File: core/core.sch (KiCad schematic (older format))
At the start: 141 parts, among them K0 KEYSW, K1 KEYSW, K10 KEYSW, K11 KEYSW, K12 KEYSW, K13 KEYSW, K14 KEYSW, K15 KEYSW, K16 KEYSW, K17 KEYSW, K18 KEYSW, K19 KEYSW, K2 KEYSW, K20 KEYSW, K21 KEYSW, K22 KEYSW, K23 KEYSW, K24 KEYSW, K25 KEYSW, K26 KEYSW, K27 KEYSW, K28 KEYSW, K29 KEYSW, K3 KEYSW, K30 KEYSW, K31 KEYSW, K32 KEYSW, K33 KEYSW, K34 KEYSW, K35 KEYSW, K36 KEYSW, K37 KEYSW, K38 KEYSW, K39 KEYSW, K4 KEYSW, K40 KEYSW, K41 KEYSW, K42 KEYSW, K43 KEYSW, K44 KEYSW, K45 KEYSW, K46 KEYSW, K47 KEYSW, K48 KEYSW, K49 KEYSW, K5 KEYSW, K50 KEYSW, K51 KEYSW, K52 KEYSW, K53 KEYSW, K54 KEYSW, K55 KEYSW, K56 KEYSW, K57 KEYSW, K58 KEYSW, K59 KEYSW, K6 KEYSW, K60 KEYSW, K61 KEYSW, K62 KEYSW, K63 KEYSW, K64 KEYSW, K65 KEYSW, K66 KEYSW, K67 KEYSW, K68 KEYSW, K69 KEYSW, K7 KEYSW, K8 KEYSW, K9 KEYSW, U1 TEENSY2.0

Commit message: finish keymatrix and assign footprints
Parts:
- D0, D1, D10, D11, D12, D13, D14, D15, D16, D17, D18, D19, D2, D20, D21, D22, D23, D24, D25, D26, D27, D28, D29, D3, D30, D31, D32, D33, D34, D35, D36, D37, D38, D39, D4, D40, D41, D42, D43, D44, D45, D46, D47, D48, D49, D5, D50, D51, D52, D53, D54, D55, D56, D57, D58, D59, D6, D60, D61, D62, D63, D64, D65, D66, D67, D68, D69, D7, D8, D9: footprint (none) -> keyboard_parts:D_SOD123_axial
- K0, K1, K10, K11, K12, K13, K14, K15, K16, K17, K18, K19, K2, K20, K21, K22, K23, K24, K25, K26, K27, K28, K29, K3, K30, K31, K32, K33, K34, K35, K36, K37, K38, K39, K4, K40, K41, K42, K43, K44, K45, K46, K47, K48, K49, K5, K50, K51, K52, K53, K54, K55, K56, K57, K58, K59, K6, K60, K61, K62, K63, K64, K65, K66, K67, K68, K69, K7, K8, K9: footprint (none) -> keyswitches:Kailh_socket
- U1: footprint (none) -> keebs:Teensy_20
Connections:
- wire segments 329 -> 439

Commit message: add an RGB controller to core
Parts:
- added U2: TLC5971PWP, Package_SO:HTSSOP-20-1EP_4.4x6.5mm_P0.65mm_EP3.4x6.5mm_Mask2.75x3.43mm_ThermalVias, symbol Driver_LED:TLC5971PWP
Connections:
- wire segments 439 -> 440
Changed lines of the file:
@@
 Wire Wire Line
 	9350 3050 10200 3050
+$Comp
+L Driver_LED:TLC5971PWP U2
+U 1 1 5DB64F07
+P 3150 4950
+F 0 "U2" H 3150 4061 50  0000 C CNN
+F 1 "TLC5971PWP" H 3150 3970 50  0000 C CNN
+F 2 "Package_SO:HTSSOP-20-1EP_4.4x6.5mm_P0.65mm_EP3.4x6.5mm_Mask2.75x3.43mm_ThermalVias" H 3200 4100 50  0001 L CNN
+F 3 "http://www.ti.com/lit/ds/symlink/tlc5971.pdf" H 3150 4650 50  0001 C CNN
+	1    3150 4950
+	1    0    0    -1
+$EndComp
+Wire Wire Line
+	2750 4850 2050 4850
 $EndSCHEMATC

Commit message: work on rgb stuff
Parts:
- added LED0, LED1, LED2, LED3, LED4, LED? (x70): LED_RGBC, symbol Device:LED_RGBC
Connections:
- net labels added: B_Zone0, G_Zone0, R_Zone0
- wire segments 440 -> 443

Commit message: update schematic with more addressable stuff
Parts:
- added D?: Inolux_IN-PI554FCH, LED_SMD:LED_Inolux_IN-PI554FCH_PLCC4_5.0x5.0mm_P3.2mm, symbol LED:Inolux_IN-PI554FCH
- D0, D1, D10, D11, D12, D13, D14, D15, D16, D17, D18, D19, D2, D20, D21, D22, D23, D24, D25, D26, D27, D28, D29, D3, D30, D31, D32, D33, D34, D35, D36, D37, D38, D39, D4, D40, D41, D42, D43, D44, D45, D46, D47, D48, D49, D5, D50, D51, D52, D53, D54, D55, D56, D57, D58, D59, D6, D60, D61, D62, D63, D64, D65, D66, D67, D68, D69, D7, D8, D9: symbol keyboard_parts:D -> core-rescue:D-keyboard_parts
- K0, K1, K10, K11, K12, K13, K14, K15, K16, K17, K18, K19, K2, K20, K21, K22, K23, K24, K25, K26, K27, K28, K29, K3, K30, K31, K32, K33, K34, K35, K36, K37, K38, K39, K4, K40, K41, K42, K43, K44, K45, K46, K47, K48, K49, K5, K50, K51, K52, K53, K54, K55, K56, K57, K58, K59, K6, K60, K61, K62, K63, K64, K65, K66, K67, K68, K69, K7, K8, K9: symbol keyboard_parts:KEYSW -> core-rescue:KEYSW-keyboard_parts
- U1: symbol keyboard_parts:TEENSY2.0 -> core-rescue:TEENSY2.0-keyboard_parts
- gave numbers to parts that had none: 29
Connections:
- net labels added: GND
- wire segments 443 -> 487
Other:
- moved on the sheet: LED0, LED1, LED10, LED11, LED12, LED13, LED14, LED15, LED16, LED17, LED18, LED19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

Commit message: add sources for LEDs and wire some in score schematic
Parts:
- removed D?: Inolux_IN-PI554FCH, LED_SMD:LED_Inolux_IN-PI554FCH_PLCC4_5.0x5.0mm_P3.2mm, symbol LED:Inolux_IN-PI554FCH
- removed LED0, LED1, LED10, LED11, LED12, LED13, LED14, LED15, LED16, LED17, LED18, LED19, LED2, LED20, LED21, LED22, LED23, LED24, LED25, LED26, LED27, LED28, LED29, LED3, LED30, LED31, LED32, LED33, LED4, LED5, LED6, LED7, LED8, LED9, LED? (x41): LED_RGBC, symbol Device:LED_RGBC
- removed U2: TLC5971PWP, Package_SO:HTSSOP-20-1EP_4.4x6.5mm_P0.65mm_EP3.4x6.5mm_Mask2.75x3.43mm_ThermalVias, symbol Driver_LED:TLC5971PWP
- added LED0, LED? (x24): WS2812, LED_SMD:LED_WS2812B_PLCC4_5.0x5.0mm_P3.2mm, symbol LED:WS2812B
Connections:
- net VCC_LED: now reaches U1.14 (VCC)
- net VCC_LED: now also LED0.3 (VSS), LED?.3 (VSS), LED?.3 (VSS), LED?.3 (VSS), LED?.3 (VSS), LED?.3 (VSS), LED?.3 (VSS), LED?.3 (VSS), LED?.3 (VSS), LED?.3 (VSS), LED?.3 (VSS), LED?.3 (VSS), LED?.3 (VSS), LED?.3 (VSS), LED?.3 (VSS), LED?.3 (VSS), LED?.3 (VSS), LED?.3 (VSS), LED?.3 (VSS), LED?.3 (VSS), LED?.3 (VSS), LED?.3 (VSS), LED?.3 (VSS), LED?.3 (VSS), LED?.3 (VSS)
- new net: LED0.2 (DOUT), LED?.4 (DIN)
- new net: LED?.2 (DOUT), LED?.4 (DIN) (x7)
- new net GND_LED: LED0.1 (VDD), LED?.1 (VDD), LED?.1 (VDD), LED?.1 (VDD), LED?.1 (VDD), LED?.1 (VDD), LED?.1 (VDD), LED?.1 (VDD), LED?.1 (VDD), LED?.1 (VDD), LED?.1 (VDD), LED?.1 (VDD), LED?.1 (VDD), LED?.1 (VDD), LED?.1 (VDD), LED?.1 (VDD), LED?.1 (VDD), LED?.1 (VDD), LED?.1 (VDD), LED?.1 (VDD), LED?.1 (VDD), LED?.1 (VDD), LED?.1 (VDD), LED?.1 (VDD), LED?.1 (VDD)

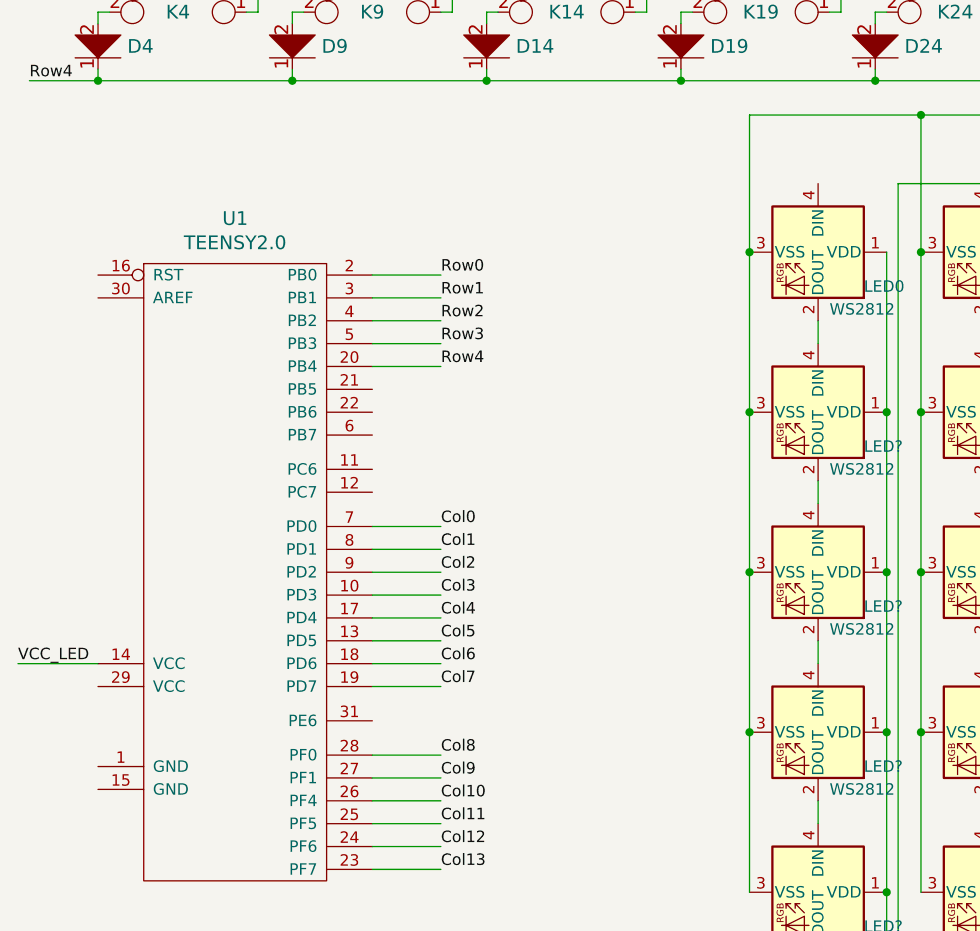
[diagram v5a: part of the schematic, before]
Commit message: update schematic
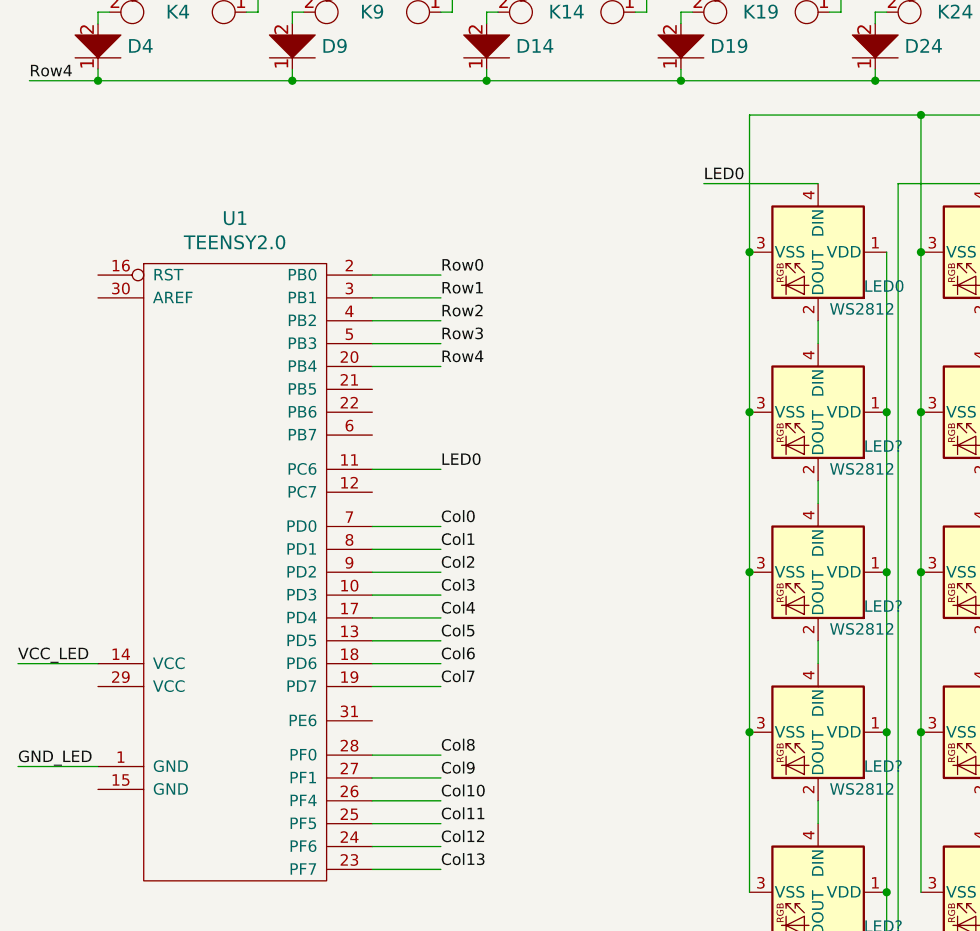
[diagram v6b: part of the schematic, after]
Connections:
- net GND_LED: now also U1.1 (GND)
- net LED0: now reaches U1.11 (PC6)
- net LED0: now also LED0.4 (DIN)
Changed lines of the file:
@@
 Wire Wire Line
 	6600 3500 7000 3500
+Text Label 2350 4750 0    50   ~ 0
+LED0
+Wire Wire Line
+	2350 4750 2050 4750
+Text Label 3500 3500 0    50   ~ 0
+LED0
+Wire Wire Line
+	3500 3500 4000 3500
+Text Label 500  6050 0    50   ~ 0
+GND_LED
+Wire Wire Line
+	500  6050 850  6050
 $EndSCHEMATC

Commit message: update schematic
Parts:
- added LED? (x45): WS2812, LED_SMD:LED_WS2812B_PLCC4_5.0x5.0mm_P3.2mm, symbol LED:WS2812B
- gave numbers to parts that had none: 4
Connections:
- net GND_LED: now also LED?.1 (VDD), LED?.1 (VDD), LED?.1 (VDD), LED?.1 (VDD), LED?.1 (VDD), LED?.1 (VDD), LED?.1 (VDD), LED?.1 (VDD), LED?.1 (VDD), LED?.1 (VDD), LED?.1 (VDD), LED?.1 (VDD), LED?.1 (VDD), LED?.1 (VDD), LED?.1 (VDD), LED?.1 (VDD), LED?.1 (VDD), LED?.1 (VDD), LED?.1 (VDD), LED?.1 (VDD), LED?.1 (VDD), LED?.1 (VDD), LED?.1 (VDD), LED?.1 (VDD), LED?.1 (VDD), LED?.1 (VDD), LED?.1 (VDD), LED?.1 (VDD), LED?.1 (VDD), LED?.1 (VDD), LED?.1 (VDD), LED?.1 (VDD), LED?.1 (VDD), LED?.1 (VDD), LED?.1 (VDD), LED?.1 (VDD), LED?.1 (VDD), LED?.1 (VDD), LED?.1 (VDD), LED?.1 (VDD), LED?.1 (VDD), LED?.1 (VDD), LED?.1 (VDD), LED?.1 (VDD), LED?.1 (VDD)
- net VCC_LED: now also LED?.3 (VSS), LED?.3 (VSS), LED?.3 (VSS), LED?.3 (VSS), LED?.3 (VSS), LED?.3 (VSS), LED?.3 (VSS), LED?.3 (VSS), LED?.3 (VSS), LED?.3 (VSS), LED?.3 (VSS), LED?.3 (VSS), LED?.3 (VSS), LED?.3 (VSS), LED?.3 (VSS), LED?.3 (VSS), LED?.3 (VSS), LED?.3 (VSS), LED?.3 (VSS), LED?.3 (VSS), LED?.3 (VSS), LED?.3 (VSS), LED?.3 (VSS), LED?.3 (VSS), LED?.3 (VSS), LED?.3 (VSS), LED?.3 (VSS), LED?.3 (VSS), LED?.3 (VSS), LED?.3 (VSS), LED?.3 (VSS), LED?.3 (VSS), LED?.3 (VSS), LED?.3 (VSS), LED?.3 (VSS), LED?.3 (VSS), LED?.3 (VSS), LED?.3 (VSS), LED?.3 (VSS), LED?.3 (VSS), LED?.3 (VSS), LED?.3 (VSS), LED?.3 (VSS), LED?.3 (VSS), LED?.3 (VSS)
- net at LED?.2 (DOUT): now also LED?.4 (DIN)
- new net: LED?.2 (DOUT), LED?.4 (DIN) (x44)

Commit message: investigate 3mm rgb leds
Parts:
- removed LED0, LED1, LED2, LED3, LED4, LED? (x65): WS2812, LED_SMD:LED_WS2812B_PLCC4_5.0x5.0mm_P3.2mm, symbol LED:WS2812B
- added LED0: LED_RCBG, Connector_PinHeader_1.00mm:PinHeader_1x04_P1.00mm_Horizontal, symbol Device:LED_RCBG
- added W0: WS2811, Package_SO:SOIC-8-1EP_3.9x4.9mm_P1.27mm_EP2.29x3mm, symbol Driver_LED:WS2811
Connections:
- net GND_LED: now also LED0.2 (K), W0.8 (VDD)
- net LED0: now also W0.6 (DIN)
- net VCC_LED: now also W0.4 (GND)
- new net: LED0.1 (RA), W0.1 (OUTR)
- new net: LED0.4 (GA), W0.2 (OUTG)
- new net: LED0.3 (BA), W0.3 (OUTB)
- no-connect marks 0 -> 1
